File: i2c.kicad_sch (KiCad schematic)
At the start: 22 parts, among them U16 PCA9517A_TSSOP, U23 TS5A3359_VSSOP, U24 TS5A3359_VSSOP

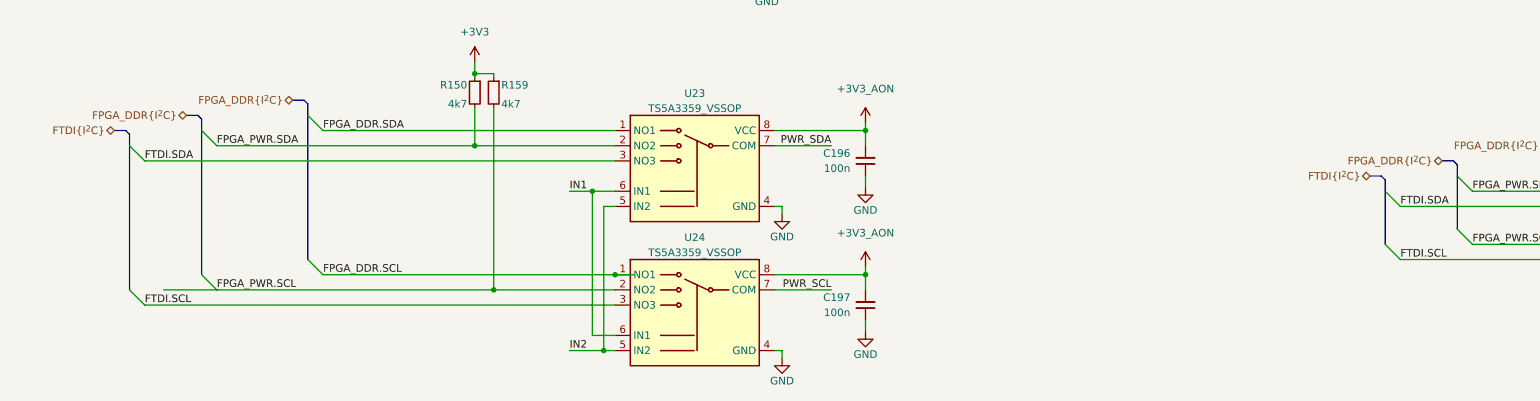
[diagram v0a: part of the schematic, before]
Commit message: Finish reconnecting signals after migration to the hierarchical structure
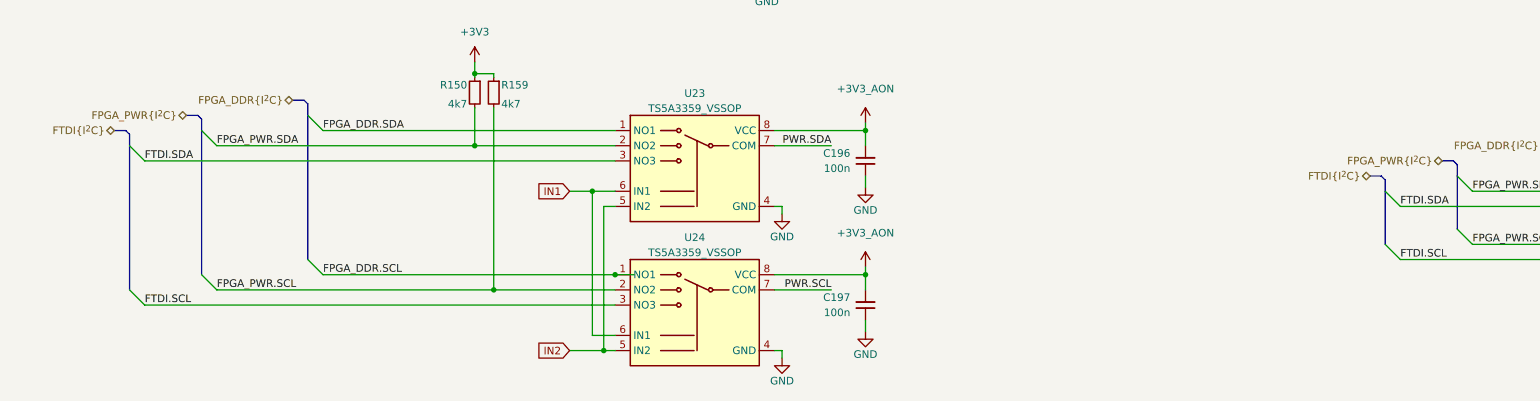
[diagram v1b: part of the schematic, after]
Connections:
- net PWR_SCL is gone; now on net PWR.SCL: U24.7 (COM)
- net PWR_SDA is gone; now on net PWR.SDA: U23.7 (COM)
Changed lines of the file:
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@@
-    (stroke (width 0) (type default) (color 0 0 0 0))
-  )
-  (wire (pts (xy 50.165 133.985) (xy 41.275 133.985))
     (stroke (width 0) (type default) (color 0 0 0 0))
   )
@@
     (effects (font (size 1.27 1.27)) (justify left bottom))
   )
-  (label "IN2" (at 109.22 144.145 0)
-    (effects (font (size 1.27 1.27)) (justify left bottom))
-  )
-  (label "PWR_SCL" (at 153.035 133.985 180)
+  (label "PWR.SCL" (at 153.035 133.985 180)
     (effects (font (size 1.27 1.27)) (justify right bottom))
   )
@@
     (effects (font (size 1.27 1.27)) (justify right bottom))
   )
-  (label "PWR_SDA" (at 153.035 109.855 180)
+  (label "PWR.SDA" (at 153.035 109.855 180)
     (effects (font (size 1.27 1.27)) (justify right bottom))
   )
@@
     (effects (font (size 1.27 1.27)) (justify left bottom))
   )
-  (label "IN1" (at 109.22 117.475 0)
-    (effects (font (size 1.27 1.27)) (justify left bottom))
+  (global_label "IN1" (shape input) (at 109.22 117.475 180) (fields_autoplaced)
+    (effects (font (size 1.27 1.27)) (justify right))
+    (property "Intersheet References" "${INTERSHEET_REFS}" (id 0) (at 103.751 117.5544 0)
+      (effects (font (size 1.27 1.27)) (justify right))
+    )
   )
   (global_label "VDDSPD" (shape input) (at 107.95 40.64 180) (fields_autoplaced)
     (effects (font (size 1.27 1.27)) (justify right))
-    (property "Intersheet References" "${INTERSHEET_REFS}" (id 0) (at -127.635 436.245 0)
-      (effects (font (size 1.27 1.27)) hide)
-    )
+    (property "Intersheet References" "${INTERSHEET_REFS}" (id 0) (at -127.635 436.245 0))
   )
   (global_label "VDDSPD" (shape input) (at 162.56 66.675 0) (fields_autoplaced)
     (effects (font (size 1.27 1.27)) (justify left))
-    (property "Intersheet References" "${INTERSHEET_REFS}" (id 0) (at -217.805 -161.29 0)
-      (effects (font (size 1.27 1.27)) hide)
-    )
+    (property "Intersheet References" "${INTERSHEET_REFS}" (id 0) (at -217.805 -161.29 0))
   )
   (global_label "VDDSPD" (shape input) (at 163.195 55.88 180) (fields_autoplaced)
     (effects (font (size 1.27 1.27)) (justify right))
     (property "Intersheet References" "${INTERSHEET_REFS}" (id 0) (at 543.56 -172.085 0)
-      (effects (font (size 1.27 1.27)) (justify left) hide)
+      (effects (font (size 1.27 1.27)) (justify left))
+    )
+  )
+  (global_label "IN2" (shape input) (at 109.22 144.145 180) (fields_autoplaced)
+    (effects (font (size 1.27 1.27)) (justify right))
+    (property "Intersheet References" "${INTERSHEET_REFS}" (id 0) (at 103.751 144.2244 0)
+      (effects (font (size 1.27 1.27)) (justify right))
     )
   )
@@
     (effects (font (size 1.27 1.27)) (justify right))
   )
+  (hierarchical_label "FPGA_PWR{I^{2}C}" (shape bidirectional) (at 45.085 104.775 180)
+    (effects (font (size 1.27 1.27)) (justify right))
+  )
   (hierarchical_label "FTDI{I^{2}C}" (shape bidirectional) (at 33.02 107.315 180)
     (effects (font (size 1.27 1.27)) (justify right))
@@
     (effects (font (size 1.27 1.27)) (justify right))
   )
-  (hierarchical_label "FPGA_DDR{I^{2}C}" (shape bidirectional) (at 255.27 112.395 180)
-    (effects (font (size 1.27 1.27)) (justify right))
-  )
-  (hierarchical_label "FPGA_DDR{I^{2}C}" (shape bidirectional) (at 45.085 104.775 180)
+  (hierarchical_label "FPGA_PWR{I^{2}C}" (shape bidirectional) (at 255.27 112.395 180)
     (effects (font (size 1.27 1.27)) (justify right))
   )
@@
   (symbol (lib_id "sodimm-ddr5-tester:+3V3_AON") (at 158.75 106.045 0) (mirror y) (unit 1)
     (in_bom yes) (on_board yes) (fields_autoplaced)
-    (property "Reference" "#PWR?" (id 0) (at 158.75 109.855 0)
+    (property "Reference" "#PWR0441" (id 0) (at 158.75 109.855 0)
       (effects (font (size 1.27 1.27)) hide)
     )
@@
   (symbol (lib_id "sodimm-ddr5-tester:GND") (at 158.75 116.84 0) (mirror y) (unit 1)
     (in_bom yes) (on_board yes) (fields_autoplaced)
-    (property "Reference" "#PWR?" (id 0) (at 158.75 123.19 0)
+    (property "Reference" "#PWR0437" (id 0) (at 158.75 123.19 0)
       (effects (font (size 1.27 1.27)) hide)
     )
@@
   (symbol (lib_id "sodimm-ddr5-tester:+3V3") (at 93.345 95.885 0) (unit 1)
     (in_bom yes) (on_board yes) (fields_autoplaced)
-    (property "Reference" "#PWR?" (id 0) (at 93.345 99.695 0)
+    (property "Reference" "#PWR0442" (id 0) (at 93.345 99.695 0)
       (effects (font (size 1.27 1.27)) hide)
     )
@@
   (symbol (lib_id "sodimm-ddr5-tester:GND") (at 144.78 121.285 0) (unit 1)
     (in_bom yes) (on_board yes)
-    (property "Reference" "#PWR?" (id 0) (at 144.78 127.635 0)
+    (property "Reference" "#PWR0436" (id 0) (at 144.78 127.635 0)
       (effects (font (size 1.27 1.27)) hide)
     )
@@
   (symbol (lib_id "sodimm-ddr5-tester:+3V3_AON") (at 158.75 130.175 0) (mirror y) (unit 1)
     (in_bom yes) (on_board yes) (fields_autoplaced)
-    (property "Reference" "#PWR?" (id 0) (at 158.75 133.985 0)
+    (property "Reference" "#PWR0440" (id 0) (at 158.75 133.985 0)
       (effects (font (size 1.27 1.27)) hide)
     )
@@
   (symbol (lib_id "sodimm-ddr5-tester:GND") (at 158.75 140.97 0) (mirror y) (unit 1)
     (in_bom yes) (on_board yes) (fields_autoplaced)
-    (property "Reference" "#PWR?" (id 0) (at 158.75 147.32 0)
+    (property "Reference" "#PWR0438" (id 0) (at 158.75 147.32 0)
       (effects (font (size 1.27 1.27)) hide)
     )
@@
   (symbol (lib_id "sodimm-ddr5-tester:GND") (at 144.78 145.415 0) (unit 1)
     (in_bom yes) (on_board yes)
-    (property "Reference" "#PWR?" (id 0) (at 144.78 151.765 0)
-      (effects (font (size 1.27 1.27)) hide)
-    )
+    (property "Reference" "#PWR0439" (id 0) (at 144.78 151.765 0)
+      (effects (font (size 1.27 1.27)) hide)
+    )

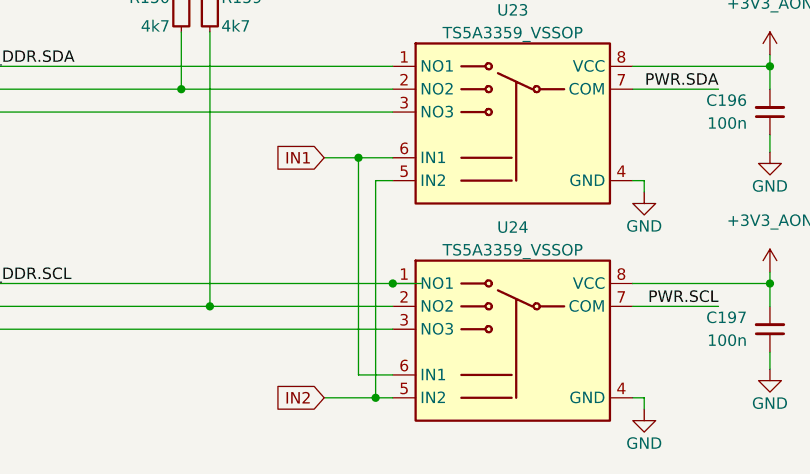
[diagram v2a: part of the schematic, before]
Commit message: Finish updating components to newest versions, improve silkscreen marking, bump revision
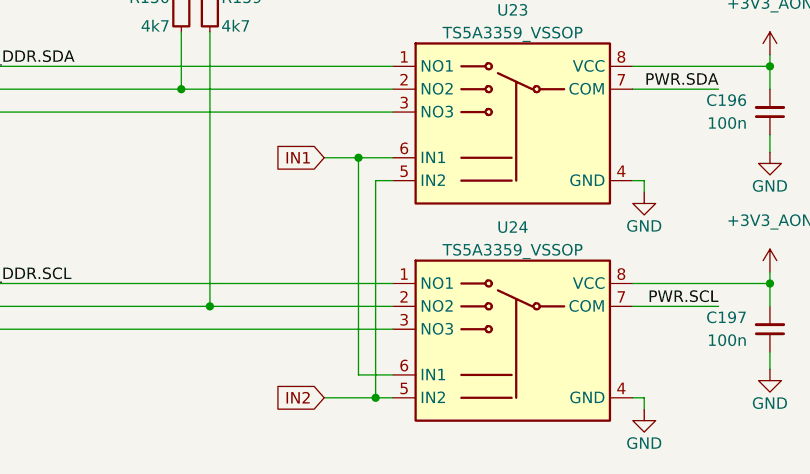
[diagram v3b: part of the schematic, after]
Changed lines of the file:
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@@
     (title_block
         (title "SO-DIMM DDR5 Tester")
-        (date "2024-01-10")
-        (rev "1.1.0")
+        (date "2024-01-18")
+        (rev "1.1.1")
         (comment 1 "www.antmicro.com")
         (comment 2 "Antmicro Ltd"))
@@
 )
     (junction
-        (at 116.84 131.445)
-        (diameter 0)
-        (color 0 0 0 0)
-)
-    (junction
         (at 158.75 107.315)
         (diameter 0)
@@
         (stroke
             (width 0)
-            (type default)
-            (color 0 0 0 0))
-)
-    (wire
-        (pts
-            (xy 116.84 131.445)
-            (xy 120.015 131.445))
-        (stroke
-            (width 0)

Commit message: Finish schematic cleanup
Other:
- note added: "0R Mux bypass"
- moved on the sheet: C165, C166, C196, C197, R122, R123, R124, R125, R126, R127, R150, R159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

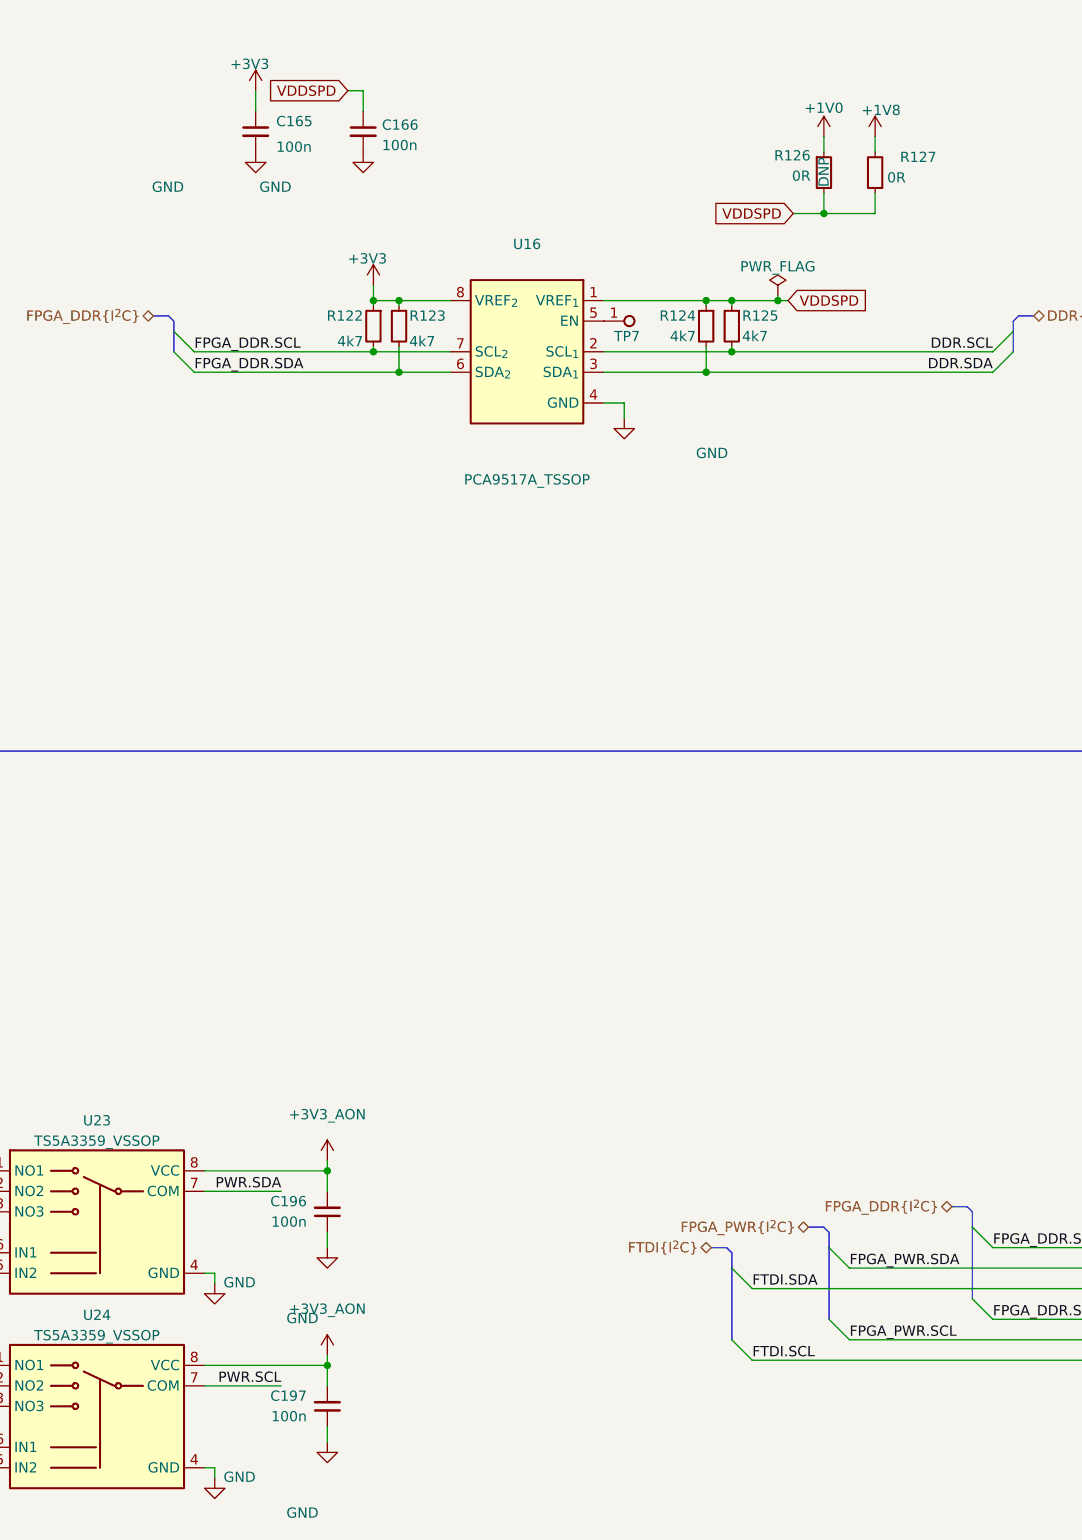
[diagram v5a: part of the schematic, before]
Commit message: Add updated components to local library
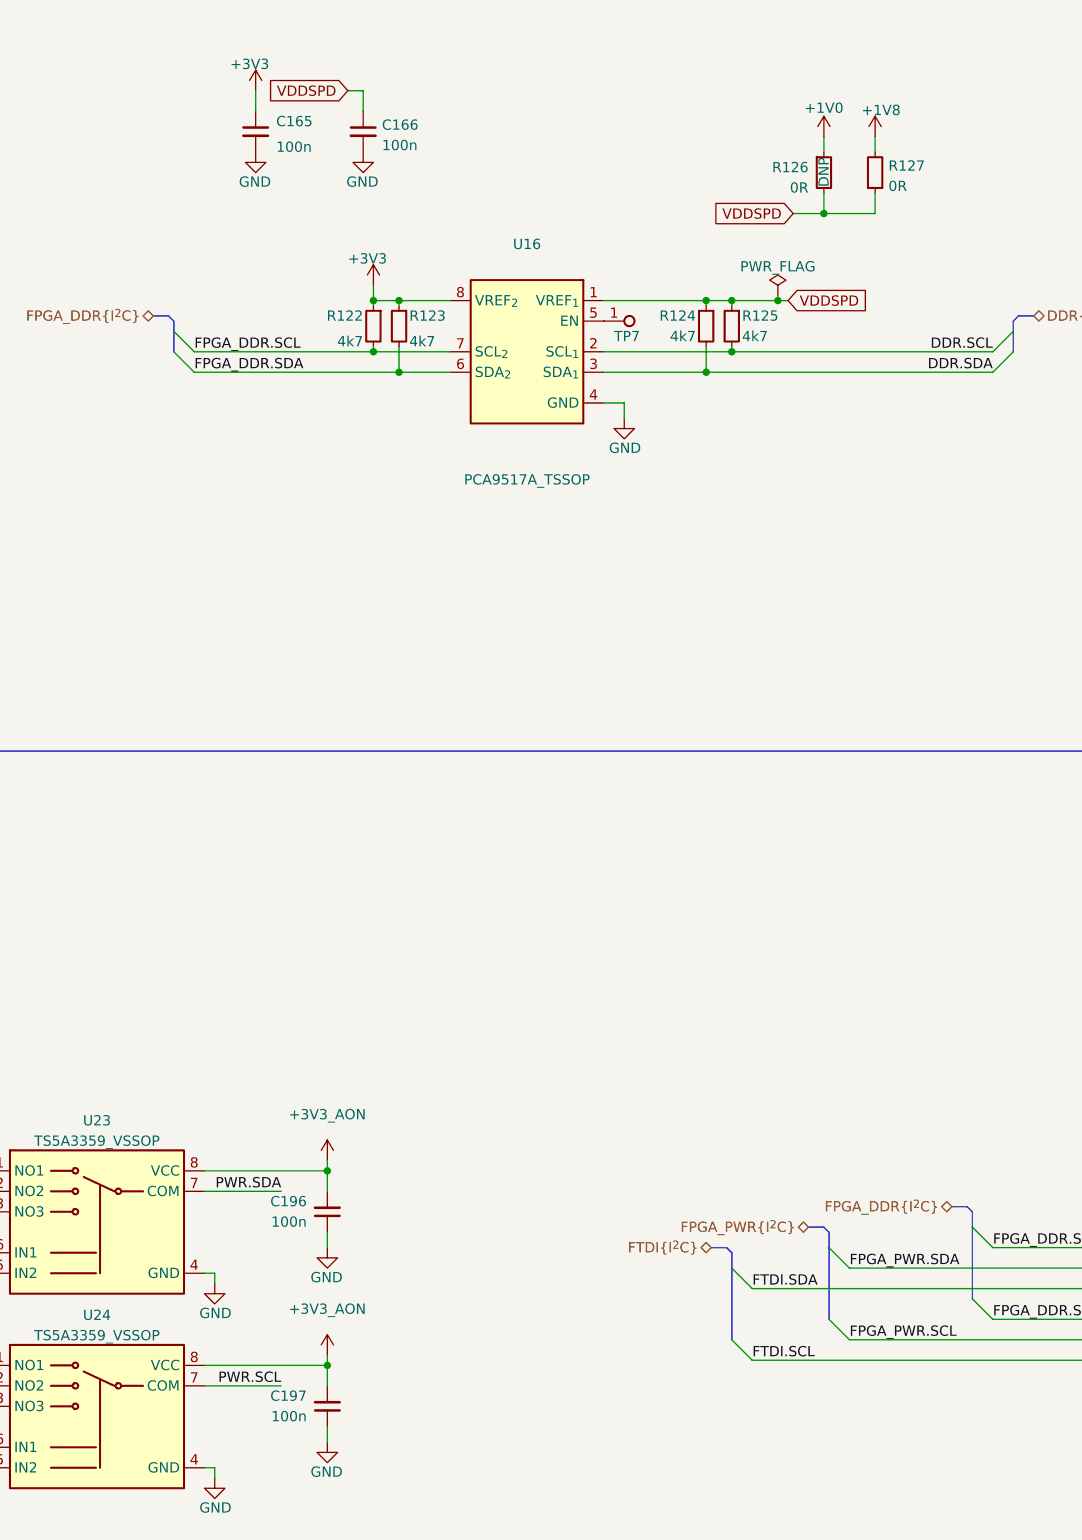
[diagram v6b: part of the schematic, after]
